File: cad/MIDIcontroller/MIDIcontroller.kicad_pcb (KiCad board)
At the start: 2 copper layers, 49 parts, among them SW1 SW_SPST, SW2 SW_SPST, SW3 SW_SPST, SW4 SW_SPST, U0 74HC595

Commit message: Started routing
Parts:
- added G***: LOGO, LOGO, F.Cu at (189.2, 50.8)
- added H1: MountingHole, MountingHole:MountingHole_4.3mm_M4, F.Cu at (73.7, 40.6)
- added H2: MountingHole, MountingHole:MountingHole_4.3mm_M4, F.Cu at (215.9, 40.6)
- added H3: MountingHole, MountingHole:MountingHole_4.3mm_M4, F.Cu at (73.7, 139.7)
- added H4: MountingHole, MountingHole:MountingHole_4.3mm_M4, F.Cu at (215.9, 139.7)
- moved R_B8 135.3 mm to (185.1, 69.2), turned to 180 degrees
- moved R_SW1 125.3 mm to (114.3, 134.6), turned to 180 degrees
- moved RV_K1 115.6 mm to (194.6, 104.1)
- moved C_SW1 109.8 mm to (104.8, 121.9)
- moved D_B8 106.8 mm to (182.5, 63.3)
- moved R_B7 101.5 mm to (174.9, 69.2), turned to 180 degrees
- moved D_SW1 99.2 mm to (116.8, 127.0)
- moved RV_K5 99.1 mm to (194.6, 83.8)
- moved C_SW2 97.8 mm to (135.3, 121.9)
- moved SW1 96.4 mm to (106.7, 127.0)
- moved R_SW2 94.8 mm to (144.8, 134.6), turned to 180 degrees
- moved D_B1 94.6 mm to (113.9, 63.3)
- moved R_ENA1 93.6 mm to (80.9, 58.5)
- moved D_B7 91.7 mm to (172.4, 63.3)
- moved SW2 86.6 mm to (137.2, 127.0)
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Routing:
- net 5V: track 0.00 -> 542.8 mm, vias 0 -> 4
- net SW4: track 0.00 -> 142.3 mm, vias 0 -> 2
- net Knob5: track 0.00 -> 120.7 mm
- net SW3: track 0.00 -> 117.9 mm
- net STCP: track 0.00 -> 114.8 mm
- net SHCP: track 0.00 -> 110.4 mm
- net Knob1: track 0.00 -> 108.7 mm
- net DS: track 0.00 -> 103.5 mm
- net Knob6: track 0.00 -> 87.3 mm
- net SW2: track 0.00 -> 85.5 mm
- net Knob2: track 0.00 -> 79.4 mm
- net Knob7: track 0.00 -> 56.1 mm
- net Encoder_A: track 0.00 -> 50.8 mm, vias 0 -> 2
- net GND: track 0.00 -> 49.8 mm, vias 0 -> 10
- net SW1: track 0.00 -> 48.4 mm
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- added copper zone on F.Cu, net 5V
- added copper zone on B.Cu, net GND
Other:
- board outline added: 157.5 x 114.3 mm
- board text added: "@andeledea/Midimine"

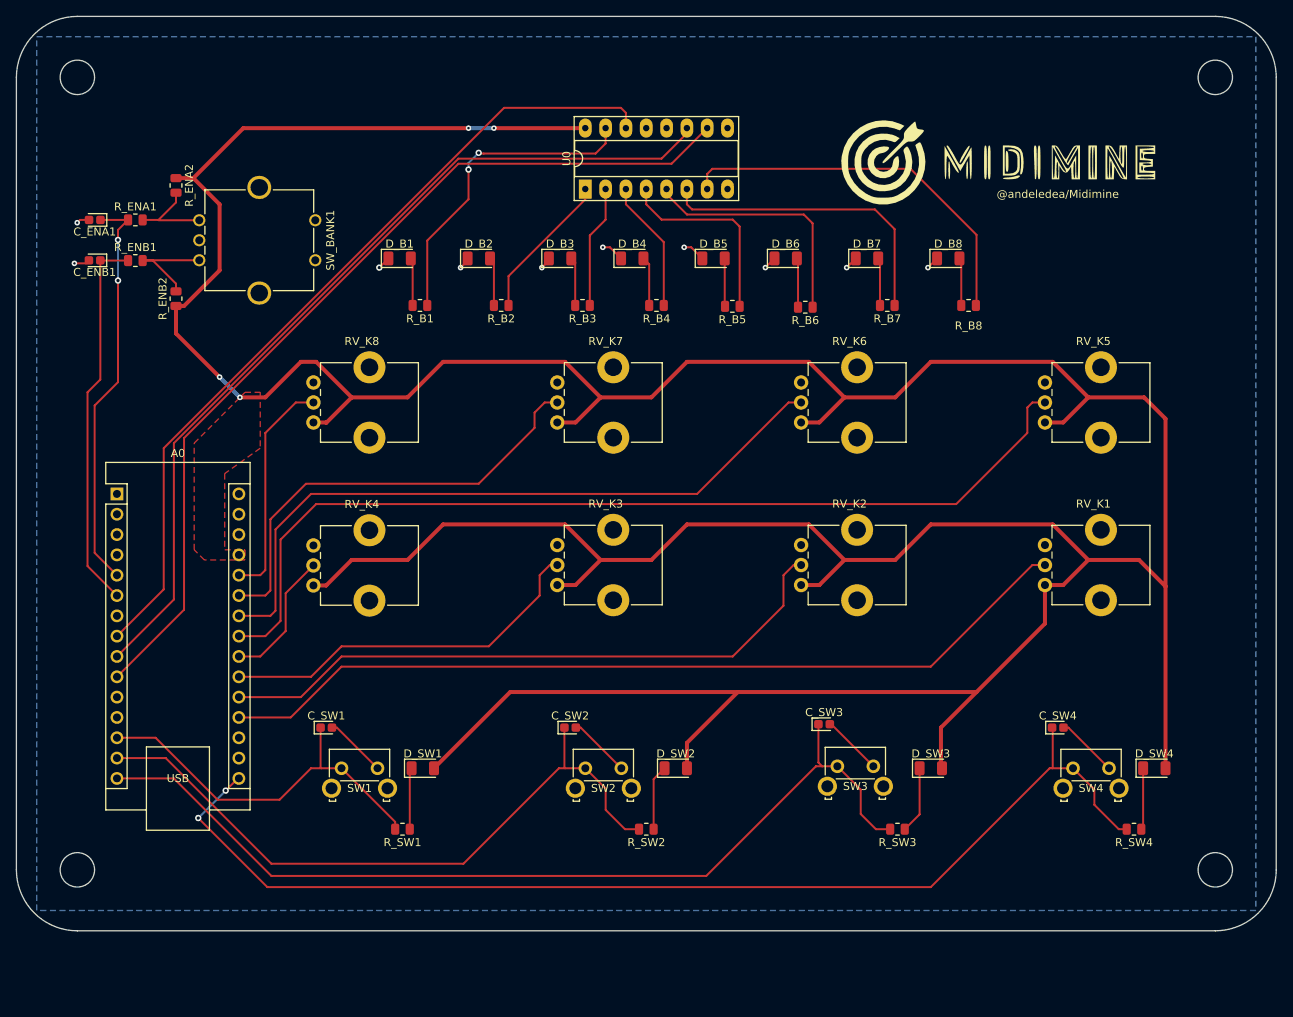
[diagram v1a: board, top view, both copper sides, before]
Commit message: added serigrafie
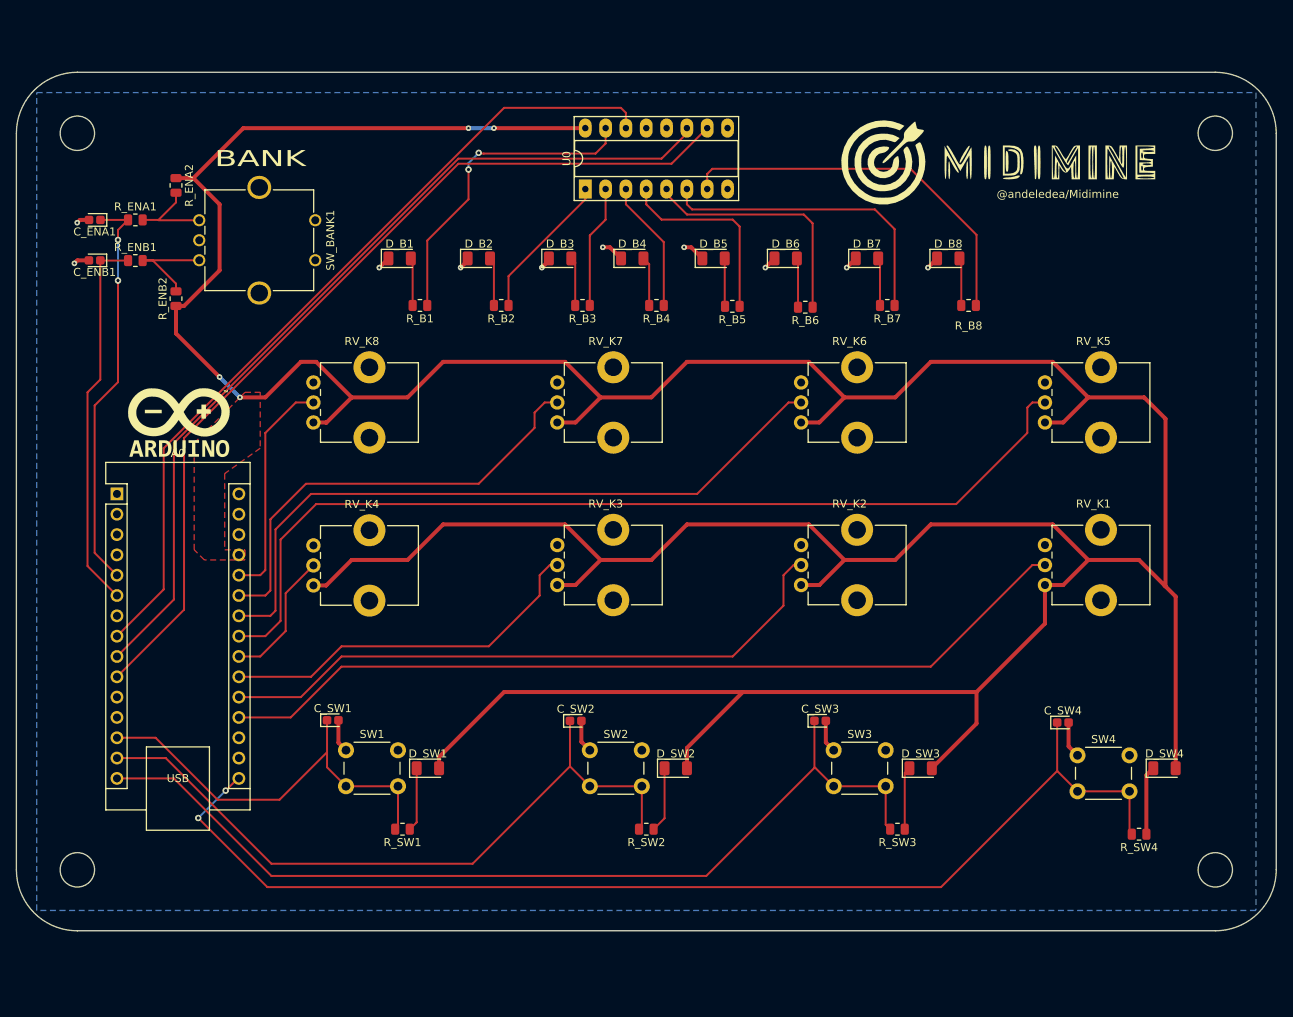
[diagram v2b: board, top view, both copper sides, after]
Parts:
- added G***: LOGO, LOGO, F.Cu at (86.4, 83.8)
- SW1, SW2, SW3, SW4: value SW_SPST -> SW_Push_Dual; footprint Button_Switch_THT:SW_SPST_Omron_B3F-315x_Angled -> Button_Switch_THT:SW_PUSH_6mm_H5mm
- moved H1 6.98 mm to (73.7, 47.6)
- moved H2 6.98 mm to (215.9, 47.6)
- moved SW2 2.32 mm to (137.7, 124.8)
- moved SW1 2.32 mm to (107.2, 124.8)
- moved SW3 2.06 mm to (168.2, 124.8)
- moved SW4 1.71 mm to (198.7, 125.4)
- moved D_SW3 1.27 mm to (179.1, 127.0)
- moved D_SW4 1.27 mm to (209.6, 127.0)
- moved C_SW1 1.22 mm to (105.6, 121.0)
- moved C_SW2 1.09 mm to (135.9, 121.1)
- moved C_SW4 0.90 mm to (196.8, 121.3)
- moved R_SW4 0.89 mm to (206.4, 135.2)
- moved C_SW3 0.66 mm to (166.5, 121.1)
- moved D_SW1 0.63 mm to (117.5, 127.0)
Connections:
- SW1 pad 1: SW1 -> GND
- SW1 pad 2: GND -> SW1
- SW2 pad 1: SW2 -> GND
- SW2 pad 2: GND -> SW2
- SW3 pad 1: SW3 -> GND
- SW3 pad 2: GND -> SW3
- SW4 pad 1: SW4 -> GND
- SW4 pad 2: GND -> SW4
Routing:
- net GND: track 49.8 -> 35.7 mm
- net SW1: track 48.4 -> 53.2 mm
- net SW4: track 142.3 -> 145.7 mm
- net SW2: track 85.5 -> 88.4 mm
- net 5V: track 542.8 -> 544.4 mm
- net SW3: track 117.9 -> 119.2 mm
- net Net-(D_SW4-Pad1): track 7.71 -> 8.79 mm
- net Net-(D_SW3-Pad1): track 8.39 -> 7.86 mm
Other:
- board size 157.5 x 114.3 mm -> 157.5 x 107.3 mm
- board text added: "BANK"

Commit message: Added button on encoder
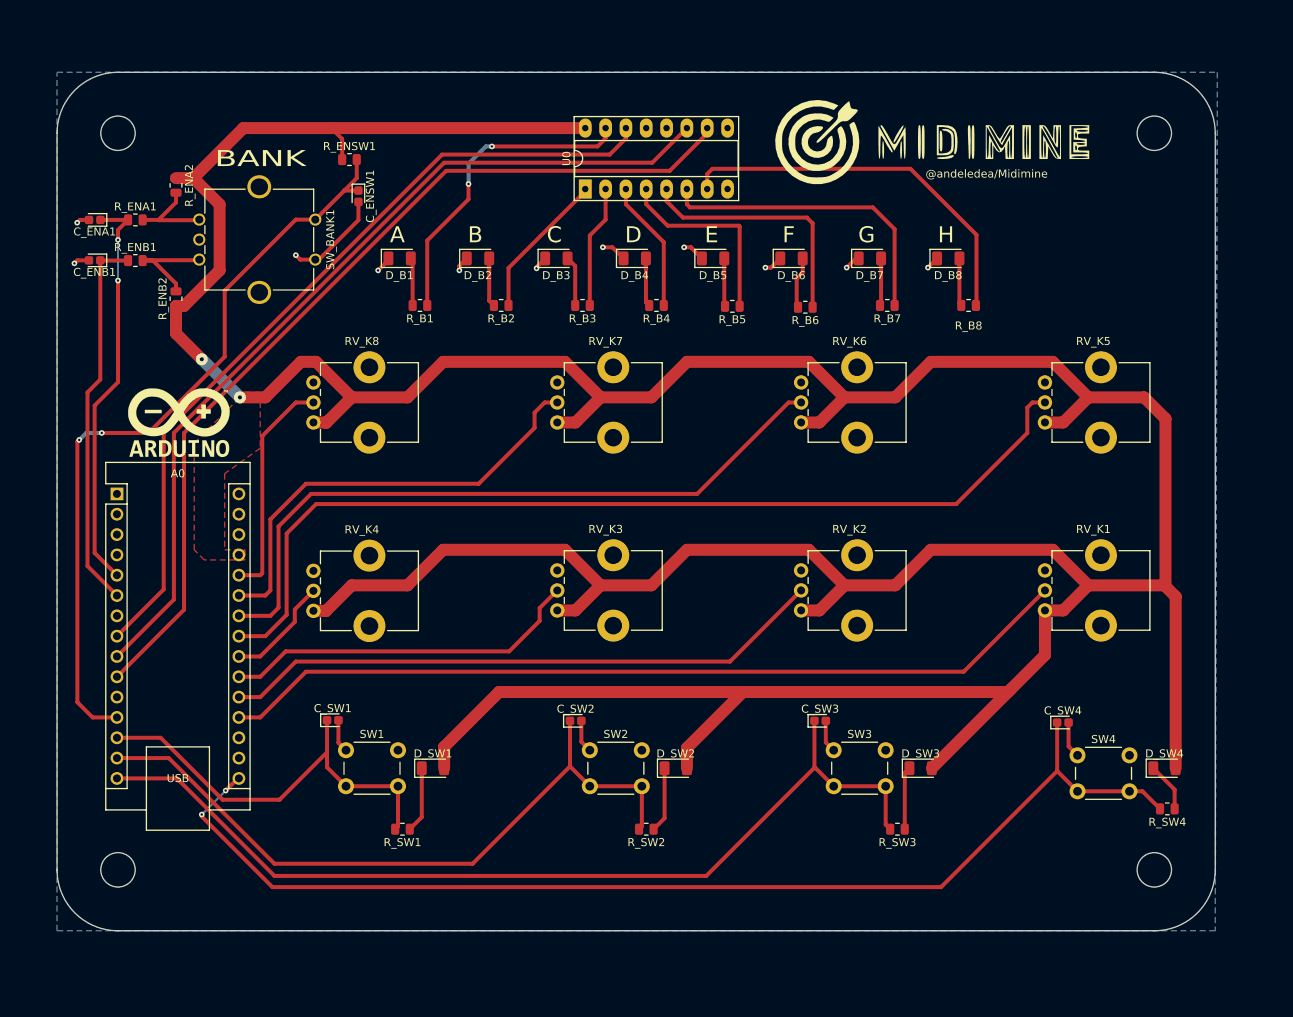
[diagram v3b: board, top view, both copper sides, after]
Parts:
- added C_ENSW1: 220n, Capacitor_Tantalum_SMD:CP_EIA-1608-08_AVX-J, F.Cu at (108.8, 55.5)
- added R_ENSW1: 10k, Resistor_SMD:R_0805_2012Metric, F.Cu at (107.7, 50.9)
- moved G*** 8.64 mm to (181.0, 48.3)
- moved H2 7.62 mm to (208.3, 47.6)
- moved H4 7.62 mm to (208.3, 139.7)
- moved H1 5.08 mm to (78.7, 47.6)
- moved H3 5.08 mm to (78.7, 139.7)
- moved R_SW4 4.74 mm to (209.9, 132.1)
- moved RV_K1 3.18 mm to (194.6, 107.3)
- moved RV_K2 3.18 mm to (164.1, 107.3)
- moved RV_K3 3.18 mm to (133.7, 107.3)
- moved RV_K4 3.17 mm to (103.2, 107.3)
- moved D_B6 0.73 mm to (162.9, 63.3)
- moved D_SW1 0.64 mm to (118.1, 127.0)
- moved D_B3 0.47 mm to (133.5, 63.3)
- moved D_B7 0.36 mm to (172.7, 63.3)
- moved D_B4 0.31 mm to (143.3, 63.3)
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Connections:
- A0 pad 12: unconnected-(A0-Pad12) -> EN_S1
- A0 pad 29: GND -> EN_S2
- A0 pad 4: GND -> EN_S2
- C_ENA1 pad 2: GND -> EN_S2
- C_ENB1 pad 2: GND -> EN_S2
- C_SW1 pad 2: GND -> EN_S2
- C_SW2 pad 2: GND -> EN_S2
- C_SW3 pad 2: GND -> EN_S2
- C_SW4 pad 2: GND -> EN_S2
- D_B1 pad 1: GND -> EN_S2
- D_B2 pad 1: GND -> EN_S2
- D_B3 pad 1: GND -> EN_S2
- D_B4 pad 1: GND -> EN_S2
- D_B5 pad 1: GND -> EN_S2
- D_B6 pad 1: GND -> EN_S2
- D_B7 pad 1: GND -> EN_S2
- D_B8 pad 1: GND -> EN_S2
- RV_K1 pad 3: GND -> EN_S2
- RV_K2 pad 3: GND -> EN_S2
- RV_K3 pad 3: GND -> EN_S2
- RV_K4 pad 3: GND -> EN_S2
- RV_K5 pad 3: GND -> EN_S2
- RV_K6 pad 3: GND -> EN_S2
- RV_K7 pad 3: GND -> EN_S2
- RV_K8 pad 3: GND -> EN_S2
- SW1 pad 1: GND -> EN_S2
- SW2 pad 1: GND -> EN_S2
- SW3 pad 1: GND -> EN_S2
- SW4 pad 1: GND -> EN_S2
- SW_BANK1 pad C: GND -> EN_S2
- SW_BANK1 pad S1: unconnected-(SW_BANK1-PadS1) -> EN_S1
- SW_BANK1 pad S2: unconnected-(SW_BANK1-PadS2) -> EN_S2
- U0 pad 8: GND -> EN_S2
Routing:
- net EN_S1: track 0.00 -> 95.8 mm, vias 0 -> 2
- net EN_S2: track 0.00 -> 50.4 mm, vias 0 -> 11
- net GND: track 35.7 -> 0.00 mm, vias 10 -> 0
- net 5V: track 544.4 -> 548.9 mm, vias 4 -> 2
- net Knob2: track 79.4 -> 75.8 mm
- net Knob4: track 16.9 -> 13.6 mm
- net Net-(D_SW4-Pad1): track 8.79 -> 6.19 mm
- net Knob3: track 47.1 -> 45.2 mm
- net SW4: track 145.7 -> 144.2 mm
- net DS: track 103.5 -> 102.1 mm
- net Knob1: track 108.7 -> 107.3 mm
- net STCP: track 114.8 -> 115.5 mm
- net Net-(R_B6-Pad1): track 30.9 -> 31.4 mm
- added copper zone on B.Cu, net EN_S2
- removed copper zone on B.Cu, net GND
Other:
- board size 157.5 x 107.3 mm -> 144.8 x 107.3 mm
- board text added: "A"
- board text added: "B"
- board text added: "C"
- board text added: "D"
- board text added: "E"
- board text added: "F"
- board text added: "G"
- board text added: "H"
